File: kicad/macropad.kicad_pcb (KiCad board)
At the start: 2 copper layers, 100 x 90 mm, 21 parts, among them J1 Conn_01x04_Pin, SW1 SW_Push, SW10 RotaryEncoder_Switch, SW2 SW_Push, SW3 SW_Push, SW4 SW_Push, SW5 SW_Push, SW6 SW_Push, SW7 SW_Push, SW8 SW_Push, SW9 SW_Push, U1 MOUDLE-SEEEDUINO-XIAO

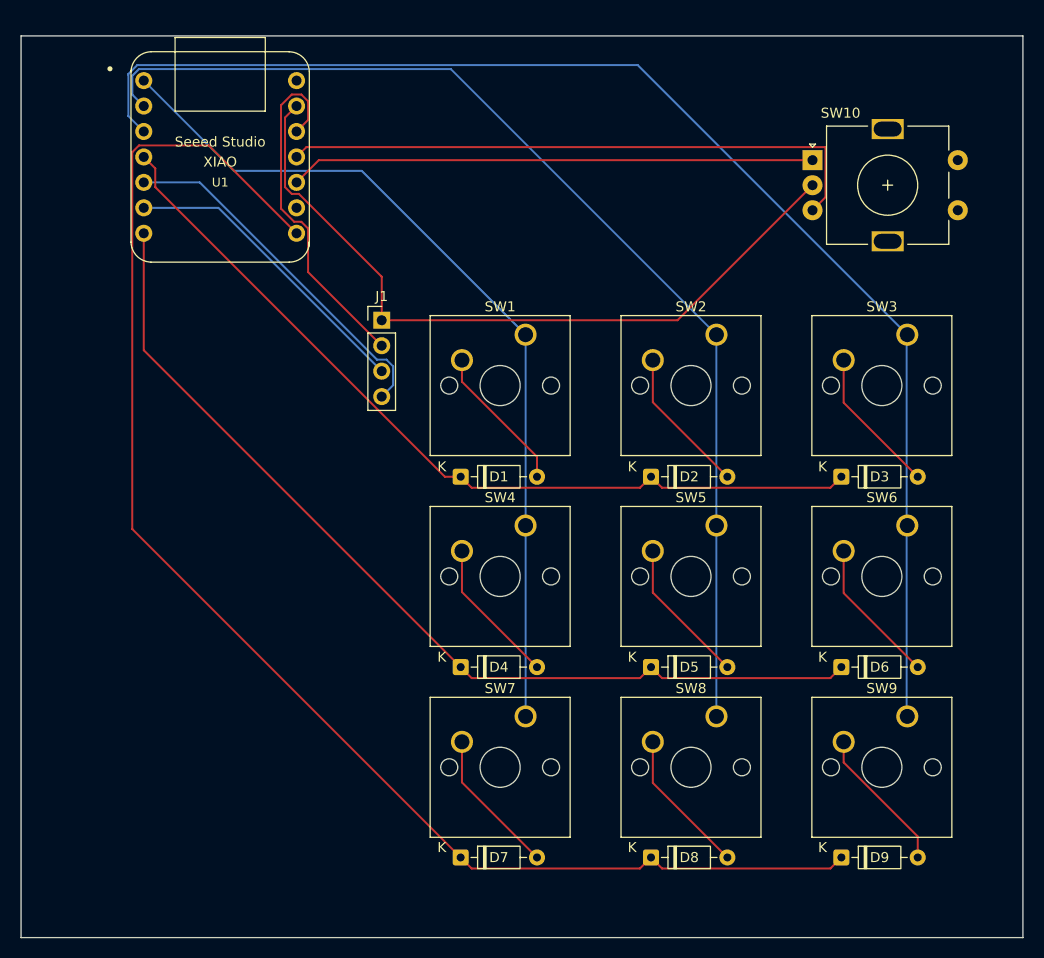
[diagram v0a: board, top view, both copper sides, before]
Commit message: add mounting holes on board
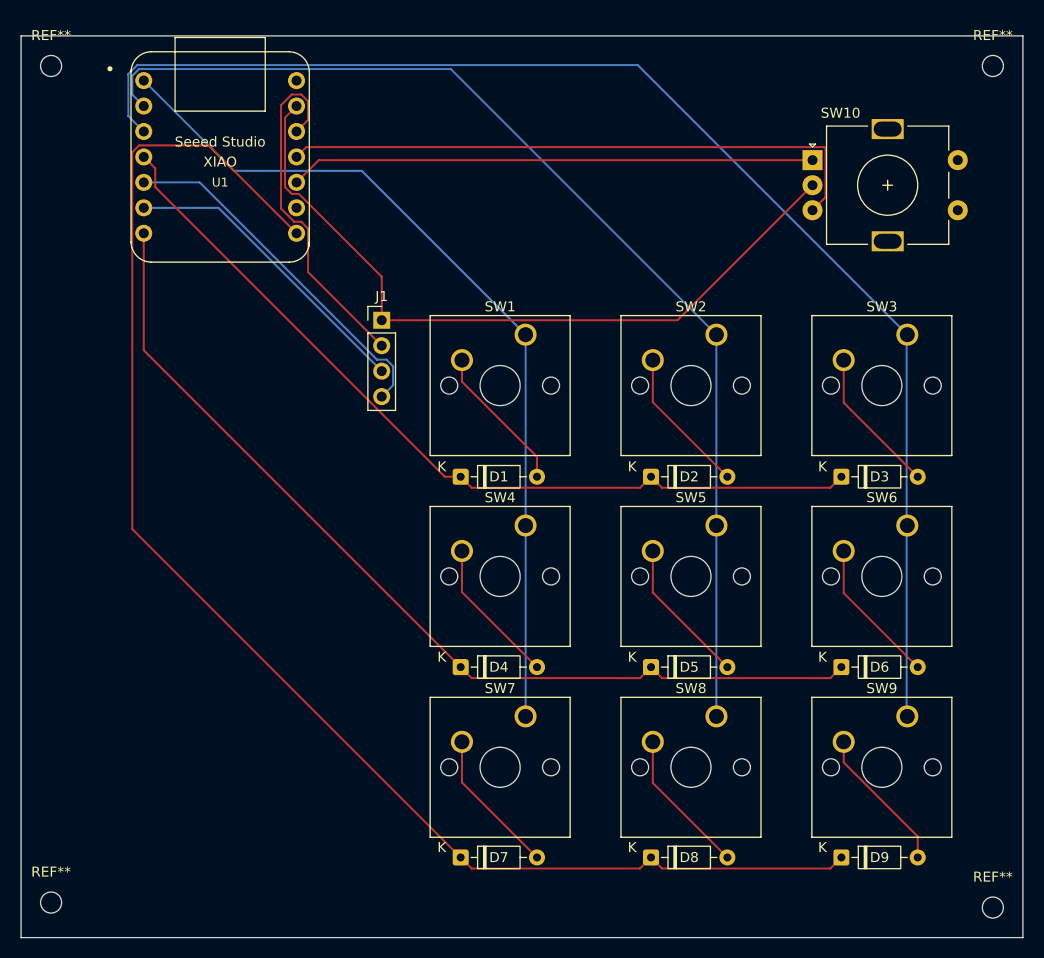
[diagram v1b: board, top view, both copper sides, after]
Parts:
- added REF**: MountingHole_2.1mm, MountingHole:MountingHole_2.1mm, F.Cu at (151.0, 53.5)
- added REF**: MountingHole_2.1mm, MountingHole:MountingHole_2.1mm, F.Cu at (245.0, 137.5)
- added REF**: MountingHole_2.1mm, MountingHole:MountingHole_2.1mm, F.Cu at (151.0, 137.0)
- added REF**: MountingHole_2.1mm, MountingHole:MountingHole_2.1mm, F.Cu at (245.0, 53.5)

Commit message: organize files
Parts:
- moved REF** 1.12 mm to (150.5, 138.0)
- moved REF** 0.71 mm to (150.5, 53.0)
- moved REF** 0.71 mm to (245.5, 138.0)
- moved REF** 0.71 mm to (245.5, 53.0)
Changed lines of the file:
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@@
 	(footprint "MountingHole:MountingHole_2.1mm"
 		(layer "F.Cu")
-		(at 151 53.5)
+		(at 150.5 53)
 		(descr "Mounting Hole 2.1mm, no annular, generated by kicad-footprint-generator mountinghole.py")
 		(tags "mountinghole")
@@
 	(footprint "MountingHole:MountingHole_2.1mm"
 		(layer "F.Cu")
-		(at 245 137.5)
+		(at 245.5 138)
 		(descr "Mounting Hole 2.1mm, no annular, generated by kicad-footprint-generator mountinghole.py")
 		(tags "mountinghole")
@@
 	(footprint "MountingHole:MountingHole_2.1mm"
 		(layer "F.Cu")
-		(at 151 137)
+		(at 150.5 138)
 		(descr "Mounting Hole 2.1mm, no annular, generated by kicad-footprint-generator mountinghole.py")
 		(tags "mountinghole")
@@
 	(footprint "MountingHole:MountingHole_2.1mm"
 		(layer "F.Cu")
-		(at 245 53.5)
+		(at 245.5 53)
 		(descr "Mounting Hole 2.1mm, no annular, generated by kicad-footprint-generator mountinghole.py")
 		(tags "mountinghole")
